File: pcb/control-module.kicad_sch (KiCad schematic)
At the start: 27 parts, among them J1 Screw_Terminal_01x08, J2 Conn_01x06_Pin, J5 Screw_Terminal_01x02, SW1 SW_DIP_x03, U1 TC2185-3.3VxCTTR

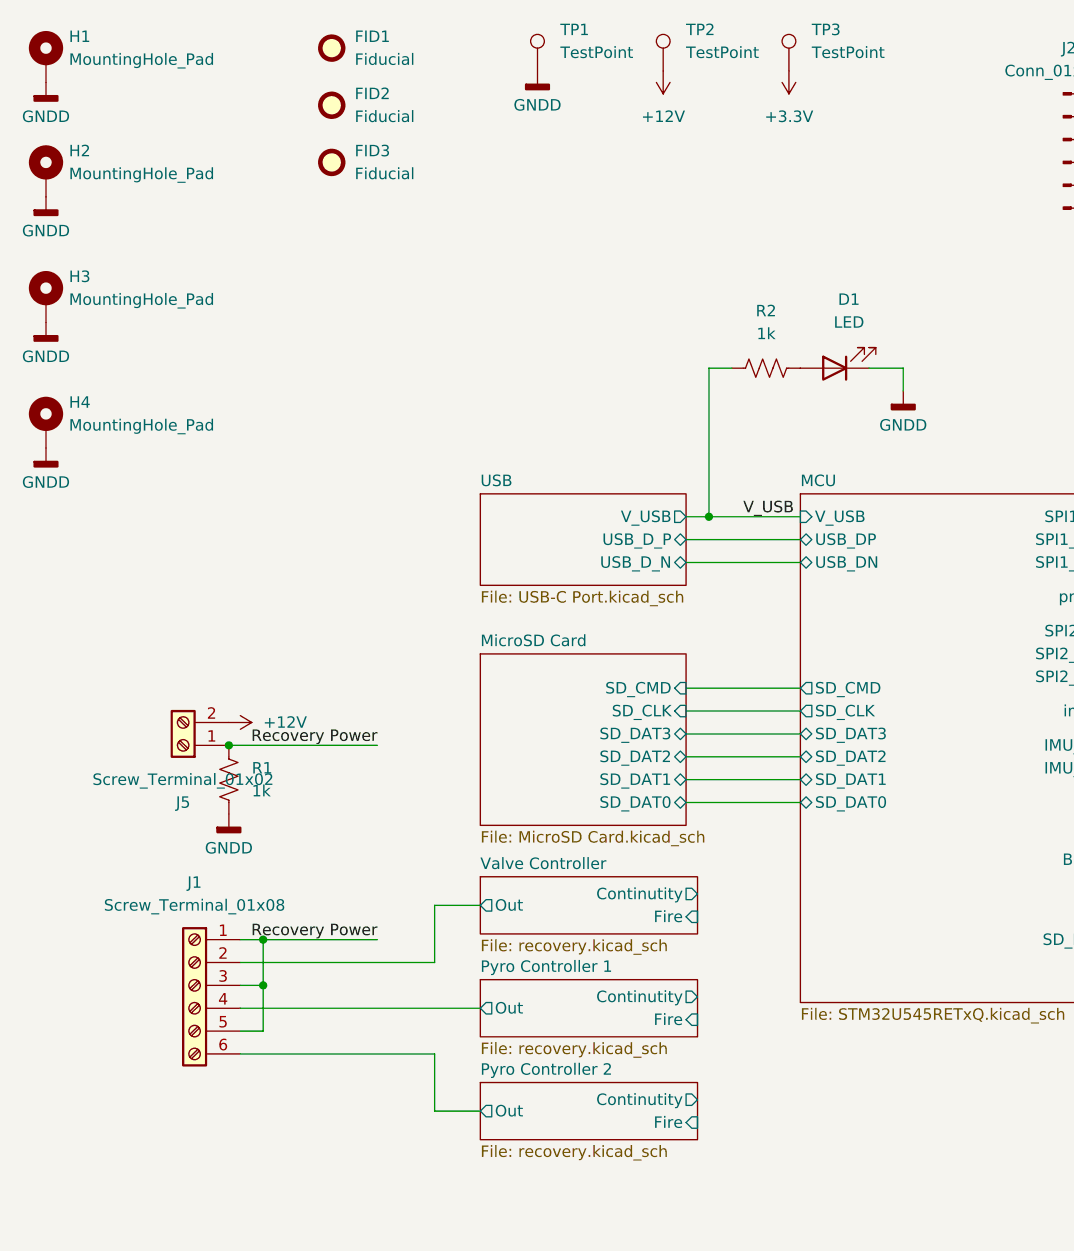
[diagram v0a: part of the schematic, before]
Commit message: Changed pin order on recovery connections
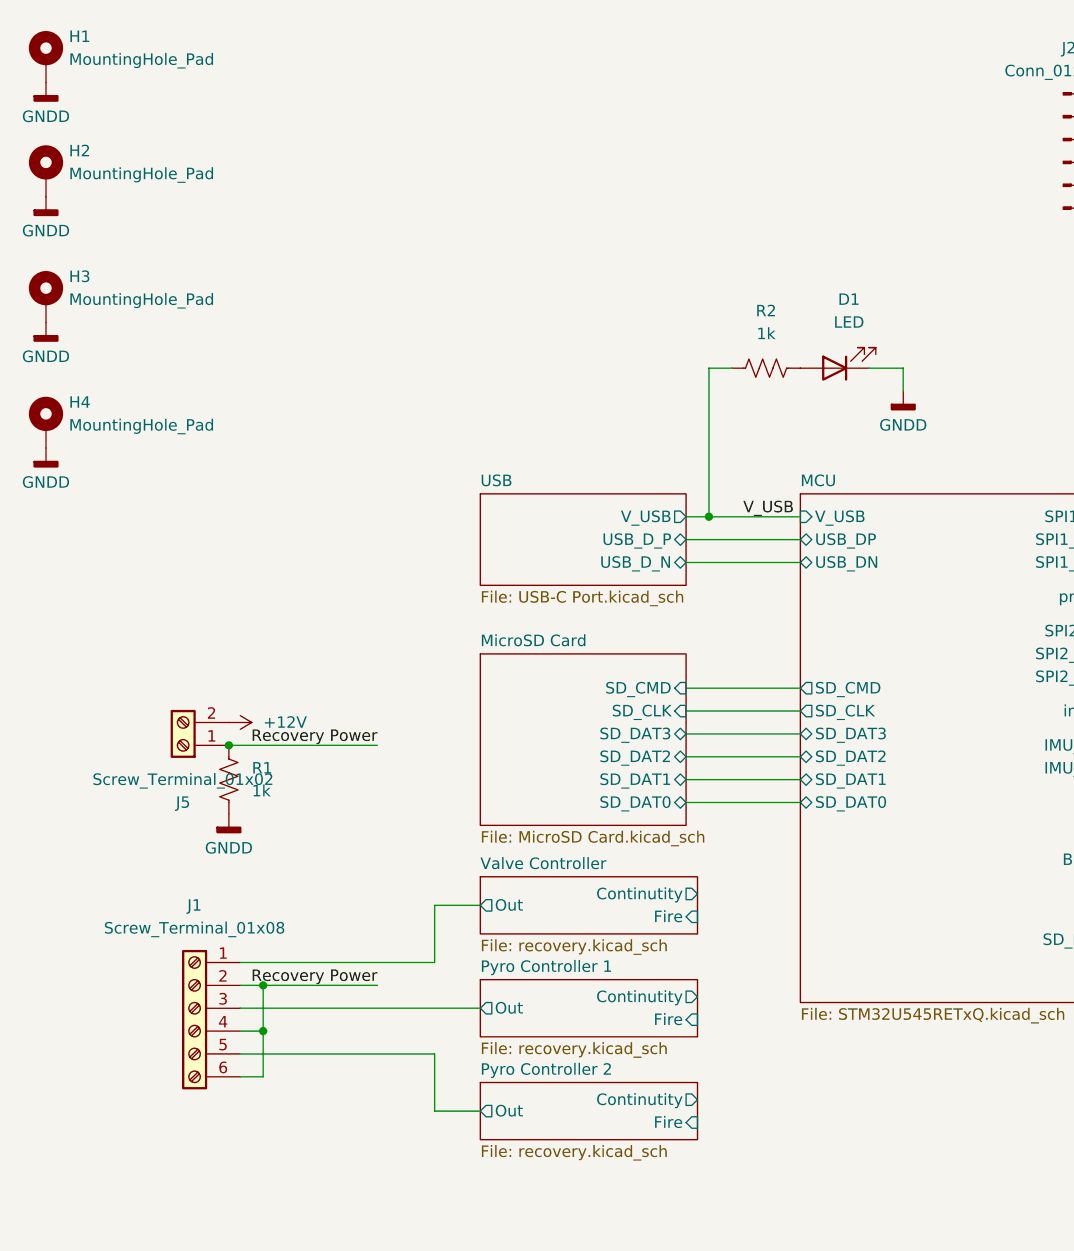
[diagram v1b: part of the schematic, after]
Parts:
- removed FID1, FID2, FID3: Fiducial, Fiducial:Fiducial_1mm_Mask3mm, symbol Mechanical:Fiducial
- removed TP1, TP2, TP3: TestPoint, TestPoint:TestPoint_Loop_D2.60mm_Drill1.6mm_Beaded, symbol Connector:TestPoint
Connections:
- net Pyro Controller 1/Out: now also J1.3 (Pin_3); no longer J1.4 (Pin_4)
- net Pyro Controller 2/Out: now also J1.5 (Pin_5); no longer J1.6 (Pin_6)
- net Recovery Power: now also J1.2 (Pin_2), J1.4 (Pin_4), J1.6 (Pin_6); no longer J1.1 (Pin_1), J1.3 (Pin_3), J1.5 (Pin_5)
- net Valve Controller/Out: now also J1.1 (Pin_1); no longer J1.2 (Pin_2)
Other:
- moved on the sheet: J1
